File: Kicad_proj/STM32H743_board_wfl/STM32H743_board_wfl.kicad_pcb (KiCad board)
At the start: 4 copper layers, 38.5 x 38.5 mm, 64 parts, among them J1 GPS, J2 ESC, J3 UART, J4 Tag_Connect_6pin, U1 LT8609SEV#PBF, U2 AP7361C-33E, U3 STM32H743VITx, U4 W25Q512JVEIQ, U5 BMI088, Y1 8MHz Crystal

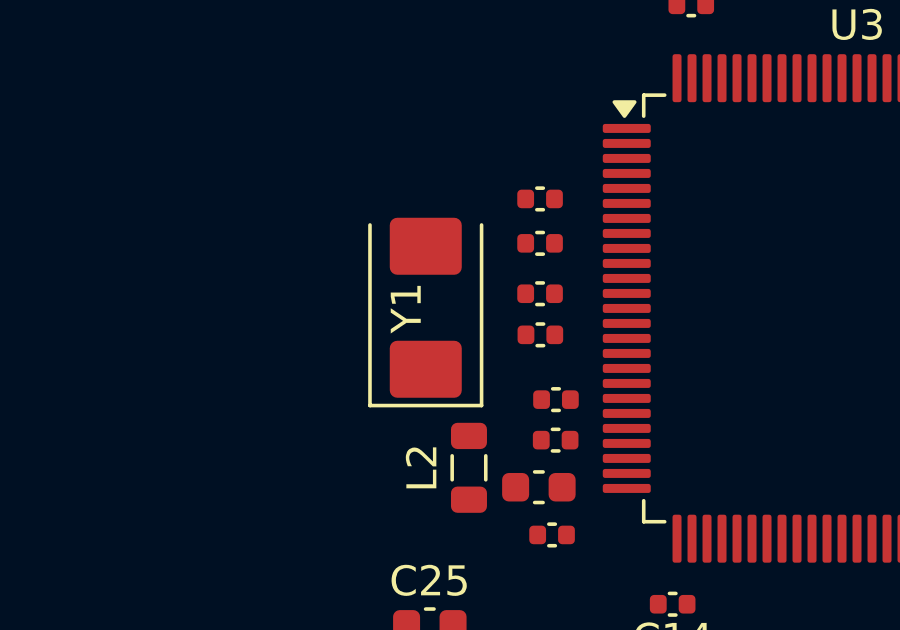
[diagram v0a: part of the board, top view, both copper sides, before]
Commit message: update stm32 quartz caps + prebom
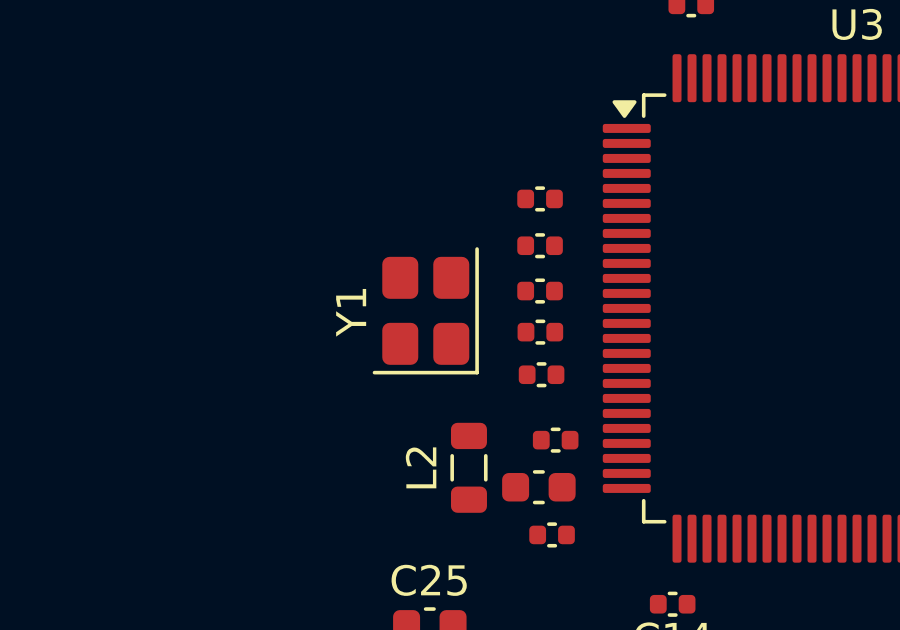
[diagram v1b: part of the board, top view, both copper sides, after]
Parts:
- C23, C24: value 27pF -> 10pF
- Y1: value 8MHz Crystal -> TSX-3225_16.0000MF18X-AC0; footprint Crystal:Crystal_SMD_Abracon_ABM3-2Pin_5.0x3.2mm -> Crystal:Crystal_SMD_3225-4Pin_3.2x2.5mm
- moved C21 0.96 mm to (46.8, 173.3)
- moved Y1 0.10 mm to (42.9, 171.1)
- moved C23 0.09 mm to (46.7, 170.5)
- moved C24 0.09 mm to (46.8, 171.8)
- moved C13 0.08 mm to (46.7, 169.0)
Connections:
- U1 pad 18: unconnected-(U1-NC_2-Pad18) -> GND
- U1 pad 19: unconnected-(U1-NC_3-Pad19) -> GND
- U1 pad 20: unconnected-(U1-NC_4-Pad20) -> GND
- U1 pad 21: unconnected-(U1-NC_5-Pad21) -> GND
- U1 pad 7: unconnected-(U1-NC_1-Pad7) -> GND
- Y1 pad 2: Net-(U3-PH0) -> GND
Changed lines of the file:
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@@
 	(footprint "Capacitor_SMD:C_0402_1005Metric"
 		(layer "F.Cu")
-		(at 46.74 170.57 180)
+		(at 46.74 170.48 180)
 		(descr "Capacitor SMD 0402 (1005 Metric), square (rectangular) end terminal, IPC-7351 nominal, (Body size source: IPC-SM-782 page 76, https://www.pcb-3d.com/wordpress/wp-content/uploads/ipc-sm-782a_amendment_1_and_2.pdf)")
 		(tags "capacitor")
@@
 			)
 		)
-		(property "Value" "27pF"
+		(property "Value" "10pF"
 			(at 0 1.16 0)
 			(layer "F.Fab")
@@
 			)
 		)
-		(property "Datasheet" "https://www.mouser.pl/pl/ProductDetail/KYOCERA-AVX/04023U270JAT2A?qs=%252BdQmOuGyFcGHQXol69SFgA%3D%3D"
+		(property "Datasheet" "https://www.tme.eu/pl/details/grm1555c1h100ga01d/kondensatory-mlcc-smd/murata/"
 			(at 0 0 0)
 			(layer "F.Fab")
@@
 	(footprint "Capacitor_SMD:C_0402_1005Metric"
 		(layer "F.Cu")
-		(at 46.75 171.94 180)
+		(at 46.75 171.85 180)
 		(descr "Capacitor SMD 0402 (1005 Metric), square (rectangular) end terminal, IPC-7351 nominal, (Body size source: IPC-SM-782 page 76, https://www.pcb-3d.com/wordpress/wp-content/uploads/ipc-sm-782a_amendment_1_and_2.pdf)")
 		(tags "capacitor")
@@
 			)
 		)
-		(property "Value" "27pF"
+		(property "Value" "10pF"
 			(at 0 1.16 0)
 			(layer "F.Fab")
@@
 			)
 		)
-		(property "Datasheet" "https://www.mouser.pl/pl/ProductDetail/KYOCERA-AVX/04023U270JAT2A?qs=%252BdQmOuGyFcGHQXol69SFgA%3D%3D"
+		(property "Datasheet" "https://www.tme.eu/pl/details/grm1555c1h100ga01d/kondensatory-mlcc-smd/murata/"
 			(at 0 0 0)
 			(layer "F.Fab")
@@
 			(size 0.25 0.7)
 			(layers "F.Cu" "F.Mask" "F.Paste")
-			(net "unconnected-(U1-NC_1-Pad7)")
+			(net "GND")
 			(pinfunction "NC_1_7")
-			(pintype "passive+no_connect")
+			(pintype "passive")
 			(thermal_bridge_angle 45)
 		)
@@
 			(size 0.375 0.375)
 			(layers "F.Cu" "F.Mask" "F.Paste")
-			(net "unconnected-(U1-NC_2-Pad18)")
+			(net "GND")
 			(pinfunction "NC_2_18")
-			(pintype "passive+no_connect")
+			(pintype "passive")
 			(thermal_bridge_angle 45)
 		)
@@
 			(size 0.375 0.375)
 			(layers "F.Cu" "F.Mask" "F.Paste")
-			(net "unconnected-(U1-NC_3-Pad19)")
+			(net "GND")
 			(pinfunction "NC_3_19")
-			(pintype "passive+no_connect")
+			(pintype "passive")
 			(thermal_bridge_angle 45)
 		)
@@
 			(size 0.375 0.375)
 			(layers "F.Cu" "F.Mask" "F.Paste")
-			(net "unconnected-(U1-NC_4-Pad20)")
+			(net "GND")
 			(pinfunction "NC_4_20")
-			(pintype "passive+no_connect")
+			(pintype "passive")
 			(thermal_bridge_angle 45)
 		)
@@
 			(size 0.375 0.375)
 			(layers "F.Cu" "F.Mask" "F.Paste")
-			(net "unconnected-(U1-NC_5-Pad21)")
+			(net "GND")
 			(pinfunction "NC_5_21")
-			(pintype "passive+no_connect")
+			(pintype "passive")
 			(thermal_bridge_angle 45)
 		)
@@
 	(footprint "Capacitor_SMD:C_0402_1005Metric"
 		(layer "F.Cu")
-		(at 46.74 168.89 180)
+		(at 46.74 168.97 180)
 		(descr "Capacitor SMD 0402 (1005 Metric), square (rectangular) end terminal, IPC-7351 nominal, (Body size source: IPC-SM-782 page 76, https://www.pcb-3d.com/wordpress/wp-content/uploads/ipc-sm-782a_amendment_1_and_2.pdf)")
 		(tags "capacitor")
@@
 		)
 	)
-	(footprint "Crystal:Crystal_SMD_Abracon_ABM3-2Pin_5.0x3.2mm"
+	(footprint "Crystal:Crystal_SMD_3225-4Pin_3.2x2.5mm"
 		(layer "F.Cu")
-		(at 42.93 171.0375 90)
-		(descr "Abracon ABM3, Miniature Ceramic Crystal, 5.0x3.2mm package, SMD, http://www.abracon.com/Resonators/abm3.pdf")
+		(at 42.93 171.14 90)
+		(descr "SMD3225/4, Crystal, 3.2x2.5mm package, SMD, http://www.txccrystal.com/images/pdf/7m-accuracy.pdf")
 		(property "Reference" "Y1"
-			(at 0 -0.63 90)
+			(at 0 -2.45 90)
 			(layer "F.SilkS")
 			(effects
@@
 			)
 		)
-		(property "Value" "8MHz Crystal"
-			(at 0 2.8 90)
+		(property "Value" "TSX-3225_16.0000MF18X-AC0"
+			(at 0 2.45 90)
 			(layer "F.Fab")
-			(hide yes)
 			(effects
 				(font
@@
 			)
 		)
-		(property "Datasheet" "https://www.mouser.pl/pl/ProductDetail/ABRACON/ABM3-8.000MHZ-D2Y-T?qs=ihRgKfnEsN4giUXjc3yS1g%3D%3D"
+		(property "Datasheet" "https://www.mouser.pl/pl/ProductDetail/Epson-Timing/TSX-3225-16.0000MF18X-AC0?qs=wwacUt%252BV97taurHtFwy%2FEA%3D%3D"
 			(at 0 0 90)
 			(layer "F.Fab")
@@
 			)
 		)
-		(property "Description" "Two pin crystal"
+		(property "Description" "Four pin crystal, GND on pins 2 and 4"
 			(at 0 0 90)
 			(layer "F.Fab")
@@
 			(unit
 				(name "A")
-				(pins "1" "2")
+				(pins "1" "2" "4" "3")
 			)
 		)
@@
 		(duplicate_pad_numbers_are_jumpers no)
 		(fp_line
-			(start 2.76 -1.86)
-			(end -3.26 -1.86)
+			(start -2.06 -1.71)
+			(end -2.06 1.71)
 			(stroke
 				(width 0.12)
@@
 		)
 		(fp_line
-			(start -3.26 -1.86)
-			(end -3.26 1.86)
+			(start -2.06 1.71)
+			(end 2.06 1.71)
 			(stroke
 				(width 0.12)
@@
 			(layer "F.SilkS")
 		)
-		(fp_line
-			(start -3.26 1.86)
-			(end 2.76 1.86)
-			(stroke
-				(width 0.12)
-				(type solid)
-			)
-			(layer "F.SilkS")
-		)
-		(fp_circle
-			(center 0 0)
-			(end 0.5 0)
-			(stroke
-				(width 0.1)
-				(type solid)
-			)
-			(fill yes)
-			(layer "F.Adhes")
-		)
 		(fp_rect
-			(start -3.25 -2.1)
-			(end 3.25 2.1)
+			(start -2.1 -1.75)
+			(end 2.1 1.75)
 			(stroke
 				(width 0.05)
@@
 		(fp_poly
 			(pts
-				(xy 2.5 -1.6) (xy 2.5 1.6) (xy -1.7 1.6) (xy -2.5 0.8) (xy -2.5 -1.6)
+				(xy 1.6 -1.25) (xy 1.6 1.25) (xy -0.975 1.25) (xy -1.6 0.625) (xy -1.6 -1.25)
 			)
 			(stroke
@@
 			(effects
 				(font
-					(size 1 1)
-					(thickness 0.15)
+					(size 0.8 0.8)
+					(thickness 0.12)
 				)
 			)
 		)
 		(pad "1" smd roundrect
-			(at -2.05 0 90)
-			(size 1.9 2.4)
+			(at -1.1 0.85 90)
+			(size 1.4 1.2)
 			(layers "F.Cu" "F.Mask" "F.Paste")
-			(roundrect_rratio 0.131579)
+			(roundrect_rratio 0.208333)
 			(net "Net-(U3-PH1)")
 			(pinfunction "1_1")
@@
 		)
 		(pad "2" smd roundrect
-			(at 2.05 0 90)
-			(size 1.9 2.4)
+			(at 1.1 0.85 90)
+			(size 1.4 1.2)
+			(layers "F.Cu" "F.Mask" "F.Paste")
+			(roundrect_rratio 0.208333)
+			(net "GND")
+			(pinfunction "G_2")
+			(pintype "passive")
+		)
+		(pad "3" smd roundrect
+			(at 1.1 -0.85 90)
+			(size 1.4 1.2)
 			(layers "F.Cu" "F.Mask" "F.Paste")
-			(roundrect_rratio 0.131579)
+			(roundrect_rratio 0.208333)
 			(net "Net-(U3-PH0)")
-			(pinfunction "2_2")
+			(pinfunction "3_3")
+			(pintype "passive")
+		)
+		(pad "4" smd roundrect
+			(at -1.1 -0.85 90)
+			(size 1.4 1.2)
+			(layers "F.Cu" "F.Mask" "F.Paste")
+			(roundrect_rratio 0.208333)
+			(net "GND")
+			(pinfunction "G_4")
 			(pintype "passive")
 		)
 		(embedded_fonts no)
-		(model "${KICAD10_3DMODEL_DIR}/Crystal.3dshapes/Crystal_SMD_Abracon_ABM3-2Pin_5.0x3.2mm.step"
+		(model "${KICAD10_3DMODEL_DIR}/Crystal.3dshapes/Crystal_SMD_3225-4Pin_3.2x2.5mm.step"
 			(offset
 				(xyz 0 0 0)
@@
 			)
 		)
-		(property "referencefab" "c19"
-			(at 0 0 90)
-			(unlocked yes)
-			(layer "F.Fab")
-			(hide yes)
-			(effects
-				(font
-					(size 1 1)
-					(thickness 0.15)
-				)
-			)
-		)
 		(property ki_fp_filters "C_*")
 		(sheetname "/03_STM32H743_schematic/")
@@
 	(footprint "Capacitor_SMD:C_0402_1005Metric"
 		(layer "F.Cu")
-		(at 47.27 174.1 180)
+		(at 46.79 173.27 180)
 		(descr "Capacitor SMD 0402 (1005 Metric), square (rectangular) end terminal, IPC-7351 nominal, (Body size source: IPC-SM-782 page 76, https://www.pcb-3d.com/wordpress/wp-content/uploads/ipc-sm-782a_amendment_1_and_2.pdf)")
 		(tags "capacitor")

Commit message: PCB v0.2 STM32 components preplaced
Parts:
- moved U4 221.0 mm to (248.2, 129.4)
- moved R13 142.8 mm to (241.8, 136.2)
- moved C29 100.2 mm to (245.8, 74.4)
- moved L3 100.2 mm to (240.4, 78.0)
- moved C27 68.7 mm to (236.2, 131.5)
- moved C28 68.7 mm to (237.3, 126.1)
- moved R8 57.4 mm to (55.1, 161.4)
- moved JP1 56.5 mm to (52.5, 161.4), turned to 180 degrees
- moved R6 52.4 mm to (53.8, 161.4)
- moved R5 50.3 mm to (47.6, 178.7)
- moved R7 50.3 mm to (56.4, 161.4), turned to 180 degrees
- moved R11 43.7 mm to (67.0, 170.8), turned to -90 degrees
- moved R10 41.0 mm to (67.0, 172.2), turned to -90 degrees
- moved R12 40.2 mm to (67.0, 169.5), turned to -90 degrees
- moved R9 36.9 mm to (67.0, 173.5), turned to -90 degrees
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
